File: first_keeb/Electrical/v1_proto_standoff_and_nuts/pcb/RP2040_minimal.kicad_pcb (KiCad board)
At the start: 4 copper layers, 67.1 x 66.8 mm, 77 parts, among them J1 Conn_01x04_Socket, P1 USB-TYPE-C-016, Q1 BSS138, SW3 TS-1187A-B-A-B, SW5 TS-1187A-B-A-B, SW6 BUTT1, SW7 BUTT3, SW8 BUTT2, U1 ME6208A44M3G, U2 ME6206A25XG, U3 PRTR5V0U2X, U5 STM32F401RCTx, U7 SLSS49E, U8 SLSS49E, U9 SLSS49E, Y1 8MHz

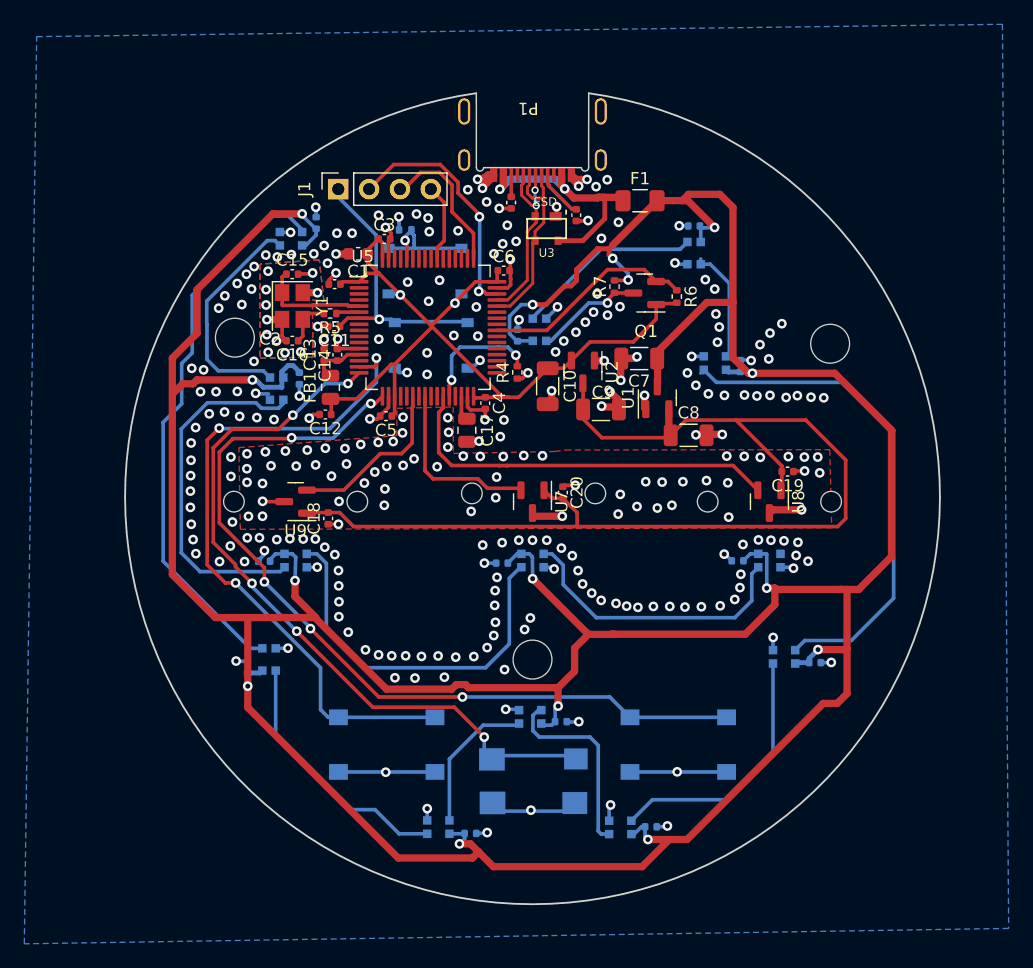
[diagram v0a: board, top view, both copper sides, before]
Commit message: changes to ws2812b 5050 and moves 5v power rail to mostly 4th layer
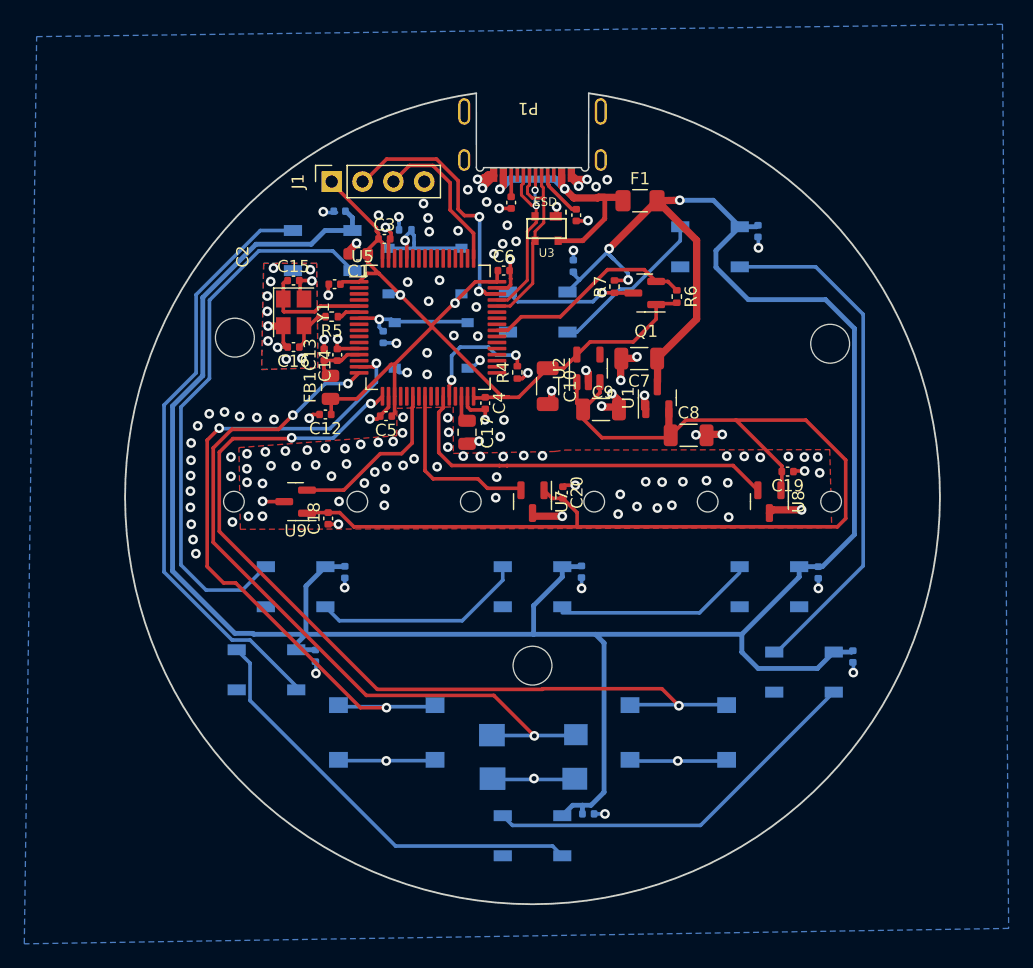
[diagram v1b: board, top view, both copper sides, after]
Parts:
- removed C30, C31, C32, C33: 100n, Capacitor_SMD:C_0402_1005Metric
- removed D10, D11, D12, D13: WS2812B-2020, LED_SMD:LED_WS2812B-2020_PLCC4_2.0x2.0mm
- C11: moved to B.Cu
- D1, D2, D3, D4, D5, D6, D7, D8, D9: value WS2812B-2020 -> WS2812B; footprint LED_SMD:LED_WS2812B-2020_PLCC4_2.0x2.0mm -> LED_SMD:LED_WS2812B_PLCC4_5.0x5.0mm_P3.2mm
- U2: value ME6206A25XG -> ME6212C33M5G; footprint Package_TO_SOT_SMD:SOT-23 -> Package_TO_SOT_SMD:SOT-23-5
- moved C25 49.8 mm to (118.6, 77.7), turned to -90 degrees
- moved D5 48.4 mm to (114.6, 79.0), turned to 180 degrees
- moved C24 38.2 mm to (103.4, 80.6), turned to 90 degrees
- moved D4 34.9 mm to (100.4, 84.4), turned to 180 degrees
- moved D2 30.5 mm to (100.0, 107.0), turned to 180 degrees
- moved C22 29.9 mm to (104.0, 105.8), turned to -90 degrees
- moved D1 29.2 mm to (80.5, 107.0), turned to 180 degrees
- moved C26 24.6 mm to (126.4, 112.8), turned to -90 degrees
- moved C21 24.1 mm to (84.5, 105.8), turned to -90 degrees
- moved D6 22.8 mm to (122.3, 114.0), turned to 180 degrees
- moved D3 18.9 mm to (119.5, 107.0), turned to 180 degrees
- moved C23 18.2 mm to (123.5, 105.8), turned to -90 degrees
- moved C27 9.83 mm to (104.6, 125.7)
- moved D7 7.79 mm to (100.0, 127.5), turned to 180 degrees
- moved C28 5.67 mm to (82.1, 112.7), turned to -90 degrees
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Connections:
- D1 pad 1: Net-(D1-DOUT) -> +5V
- D1 pad 2: GND -> Net-(D1-DOUT)
- D1 pad 3: Net-(D1-DIN) -> GND
- D1 pad 4: +5V -> UG_DIN
- D2 pad 1: Net-(D2-DOUT) -> +5V
- D2 pad 2: GND -> Net-(D2-DOUT)
- D2 pad 3: Net-(D1-DOUT) -> GND
- D2 pad 4: +5V -> Net-(D1-DOUT)
- D3 pad 1: Net-(D3-DOUT) -> +5V
- D3 pad 2: GND -> unconnected-(D3-DOUT-Pad2)
- D3 pad 3: Net-(D2-DOUT) -> GND
- D3 pad 4: +5V -> Net-(D2-DOUT)
- D4 pad 1: Net-(D4-DOUT) -> +5V
- D4 pad 2: GND -> Net-(D4-DOUT)
- D4 pad 3: Net-(D3-DOUT) -> GND
- D4 pad 4: +5V -> Net-(D4-DIN)
- D5 pad 1: Net-(D5-DOUT) -> +5V
- D5 pad 2: GND -> Net-(D5-DOUT)
- D5 pad 3: Net-(D4-DOUT) -> GND
- D5 pad 4: +5V -> Net-(D4-DOUT)
- D6 pad 1: Net-(D6-DOUT) -> +5V
- D6 pad 2: GND -> Net-(D6-DOUT)
- D6 pad 3: Net-(D5-DOUT) -> GND
- D6 pad 4: +5V -> Net-(D5-DOUT)
- D7 pad 1: Net-(D7-DOUT) -> +5V
- D7 pad 2: GND -> Net-(D7-DOUT)
- D7 pad 3: Net-(D6-DOUT) -> GND
- D7 pad 4: +5V -> Net-(D6-DOUT)
- D8 pad 1: Net-(D8-DOUT) -> +5V
- D8 pad 2: GND -> Net-(D8-DOUT)
- D8 pad 3: Net-(D7-DOUT) -> GND
- D8 pad 4: +5V -> Net-(D7-DOUT)
- D9 pad 1: Net-(D10-DIN) -> +5V
- D9 pad 2: GND -> UG_DIN
- D9 pad 3: Net-(D8-DOUT) -> GND
- D9 pad 4: +5V -> Net-(D8-DOUT)
- J1 pad 1: NRST -> VDD
- J1 pad 4: SWO -> GND
- Q1 pad 3: Net-(D1-DIN) -> Net-(D4-DIN)
- R7 pad 1: Net-(D1-DIN) -> Net-(D4-DIN)
- U2 pad 1: GND -> +4V4
- U2 pad 2: VDD -> GND
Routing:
- net +5V: track 334.4 -> 229.8 mm, vias 15 -> 3
- net UG_DIN: track 0.00 -> 45.5 mm
- net Net-(D3-DOUT): track 41.7 -> 0.00 mm
- net Net-(D11-DOUT): track 31.2 -> 0.00 mm
- net Net-(D10-DOUT): track 29.4 -> 0.00 mm
- net Net-(D5-DOUT): track 16.1 -> 42.7 mm
- net Net-(D12-DOUT): track 23.8 -> 0.00 mm
- net Net-(D6-DOUT): track 12.0 -> 32.1 mm
- net Net-(D10-DIN): track 18.9 -> 0.00 mm
- net GND: track 113.7 -> 95.9 mm, vias 294 -> 158
- net Net-(D7-DOUT): track 21.1 -> 35.6 mm
- net NRST: track 23.1 -> 10.3 mm
- net Net-(D4-DIN): track 0.00 -> 10.9 mm, vias 0 -> 1
- net Net-(D1-DIN): track 8.94 -> 0.00 mm, vias 1 -> 0
- net Net-(D4-DOUT): track 21.3 -> 13.5 mm
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
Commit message: v1 stm ordered
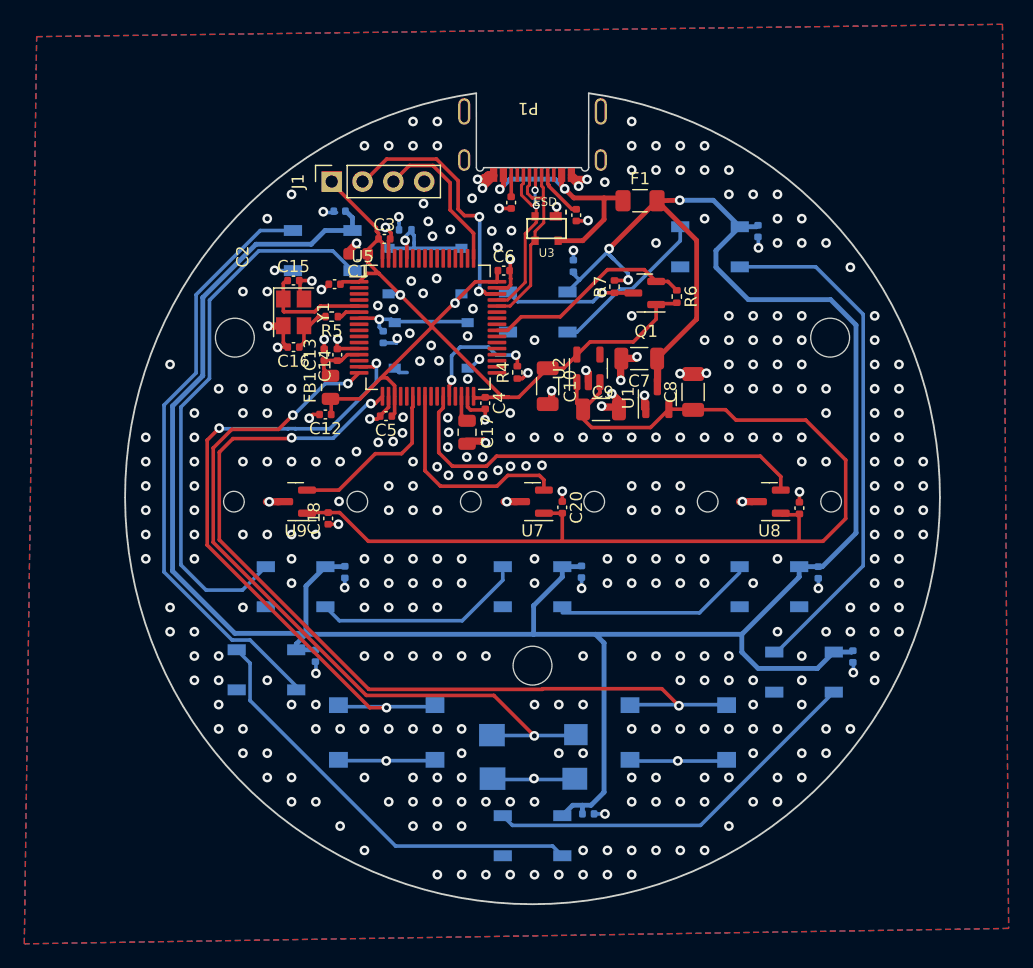
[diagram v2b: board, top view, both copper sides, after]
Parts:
- U2: value ME6212C33M5G -> ME6212C25M5G
- moved C8 3.59 mm to (113.2, 91.0), turned to 90 degrees
- moved C19 3.16 mm to (122.0, 100.5), turned to -90 degrees
- moved C20 1.22 mm to (102.5, 100.5)
- moved H1 0.50 mm to (124.5, 86.5)
- turned U7 to 180 degrees
- turned U8 to 180 degrees
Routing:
- net +4V4: track 93.4 -> 88.0 mm
- net ADC_IN3: track 32.3 -> 35.6 mm
- net ADC_IN2: track 14.7 -> 17.8 mm
- net BUTT0: track 57.2 -> 56.2 mm
- net GND: track 95.9 -> 95.3 mm, vias 158 -> 376

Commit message: updates pcb
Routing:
- net Net-(D2-DOUT): track 16.0 -> 17.0 mm
- net GND: track 95.3 -> 95.6 mm, vias 376 -> 381
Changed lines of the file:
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@@
   (segment (start 78.29 99.97) (end 78.24 99.97) (width 0.3) (layer "F.Cu") (net 1))
   (segment (start 103.8 73.95) (end 103.72 73.87) (width 0.3) (layer "F.Cu") (net 1))
+  (segment (start 101.854 75.692) (end 101.985023 75.823023) (width 0.4) (layer "F.Cu") (net 1))
   (segment (start 103.569466 73.474466) (end 103.2 73.105) (width 0.6) (layer "F.Cu") (net 1))
   (segment (start 101.575 90.875) (end 101.575 91.943813) (width 0.6) (layer "F.Cu") (net 1))
@@
   (segment (start 88.355 77.88) (end 88.355 78.3) (width 0.3) (layer "F.Cu") (net 1))
   (segment (start 104.375 76.895) (end 104.57 76.86) (width 0.3) (layer "F.Cu") (net 1))
+  (segment (start 101.985023 75.823023) (end 101.985023 76.325023) (width 0.4) (layer "F.Cu") (net 1))
   (segment (start 98.17 80.05) (end 98.17 81.168959) (width 0.3) (layer "F.Cu") (net 1))
   (segment (start 98.242 75.863) (end 97.313 75.863) (width 0.3) (layer "F.Cu") (net 1))
@@
   (segment (start 96.8 73.22) (end 95.88 74.14) (width 0.6) (layer "F.Cu") (net 1))
   (segment (start 97.951041 82.4) (end 97.075 82.4) (width 0.3) (layer "F.Cu") (net 1))
-  (segment (start 101.985023 75.724977) (end 101.985023 76.325023) (width 0.4) (layer "F.Cu") (net 1))
   (segment (start 106.5275 91.1025) (end 107.04 91.615) (width 0.6) (layer "F.Cu") (net 1))
   (segment (start 81.808258 81.798258) (end 80.802728 81.798258) (width 0.3) (layer "F.Cu") (net 1))
@@
   (via (at 90.166 108.706) (size 0.8) (drill 0.4) (layers "F.Cu" "B.Cu") (free) (net 1))
   (via (at 124.166 118.706) (size 0.8) (drill 0.4) (layers "F.Cu" "B.Cu") (free) (net 1))
+  (via (at 108.166 108.706) (size 0.8) (drill 0.4) (layers "F.Cu" "B.Cu") (free) (net 1))
   (via (at 101.575 90.875) (size 0.8) (drill 0.4) (layers "F.Cu" "B.Cu") (net 1))
   (via (at 100.166 104.706) (size 0.8) (drill 0.4) (layers "F.Cu" "B.Cu") (free) (net 1))
@@
   (via (at 90.166 70.706) (size 0.8) (drill 0.4) (layers "F.Cu" "B.Cu") (free) (net 1))
   (via (at 117.28 100) (size 0.8) (drill 0.4) (layers "F.Cu" "B.Cu") (net 1))
+  (via (at 112.166 108.706) (size 0.8) (drill 0.4) (layers "F.Cu" "B.Cu") (free) (net 1))
+  (via (at 104.166 108.706) (size 0.8) (drill 0.4) (layers "F.Cu" "B.Cu") (free) (net 1))
   (via (at 100.166 106.706) (size 0.8) (drill 0.4) (layers "F.Cu" "B.Cu") (free) (net 1))
   (via (at 76.166 92.706) (size 0.8) (drill 0.4) (layers "F.Cu" "B.Cu") (free) (net 1))
-  (via (at 103.37 79.3195) (size 0.8) (drill 0.4) (layers "F.Cu" "B.Cu") (net 1))
+  (via (at 104.394 80.01) (size 0.8) (drill 0.4) (layers "F.Cu" "B.Cu") (net 1))
   (via (at 68.166 104.706) (size 0.8) (drill 0.4) (layers "F.Cu" "B.Cu") (free) (net 1))
   (via (at 72.166 96.706) (size 0.8) (drill 0.4) (layers "F.Cu" "B.Cu") (free) (net 1))
@@
   (via (at 91 82.85) (size 0.8) (drill 0.4) (layers "F.Cu" "B.Cu") (free) (net 1))
   (via (at 87.27 83.86) (size 0.8) (drill 0.4) (layers "F.Cu" "B.Cu") (free) (net 1))
-  (via (at 101.985023 75.724977) (size 0.8) (drill 0.4) (layers "F.Cu" "B.Cu") (net 1))
+  (via (at 101.854 75.692) (size 0.8) (drill 0.4) (layers "F.Cu" "B.Cu") (net 1))
   (via (at 78.166 82.706) (size 0.8) (drill 0.4) (layers "F.Cu" "B.Cu") (free) (net 1))
   (via (at 108.166 94.706) (size 0.8) (drill 0.4) (layers "F.Cu" "B.Cu") (free) (net 1))
@@
   (via (at 82.85 86.64) (size 0.8) (drill 0.4) (layers "F.Cu" "B.Cu") (net 1))
   (via (at 108.166 68.706) (size 0.8) (drill 0.4) (layers "F.Cu" "B.Cu") (free) (net 1))
+  (via (at 106.166 108.706) (size 0.8) (drill 0.4) (layers "F.Cu" "B.Cu") (free) (net 1))
   (via (at 82.166 116.706) (size 0.8) (drill 0.4) (layers "F.Cu" "B.Cu") (free) (net 1))
   (via (at 114.3125 89.4275) (size 0.8) (drill 0.4) (layers "F.Cu" "B.Cu") (net 1))
@@
   (via (at 118.166 124.706) (size 0.8) (drill 0.4) (layers "F.Cu" "B.Cu") (free) (net 1))
   (via (at 120.166 94.706) (size 0.8) (drill 0.4) (layers "F.Cu" "B.Cu") (free) (net 1))
+  (via (at 110.166 108.706) (size 0.8) (drill 0.4) (layers "F.Cu" "B.Cu") (free) (net 1))
   (via (at 78.166 92.706) (size 0.8) (drill 0.4) (layers "F.Cu" "B.Cu") (free) (net 1))
   (via (at 68.166 100.706) (size 0.8) (drill 0.4) (layers "F.Cu" "B.Cu") (free) (net 1))
@@
   (segment (start 123.535 106.245) (end 123.535 107.135) (width 0.3) (layer "B.Cu") (net 1))
   (segment (start 123.535 107.145) (end 123.535 107.195) (width 0.3) (layer "B.Cu") (net 1))
-  (segment (start 103.37 79.3195) (end 103.37 80.18) (width 0.3) (layer "B.Cu") (net 1))
   (segment (start 126.41 114.07) (end 126.415 114.075) (width 0.3) (layer "B.Cu") (net 1))
   (segment (start 88.86 86.56) (end 88.8 86.96) (width 0.3) (layer "B.Cu") (net 1))
   (segment (start 87.9425 121.32) (end 84.0675 121.32) (width 0.3) (layer "B.Cu") (net 1))
-  (segment (start 103.37 80.18) (end 103.36 80.19) (width 0.3) (layer "B.Cu") (net 1))
+  (segment (start 103.54 80.01) (end 103.36 80.19) (width 0.3) (layer "B.Cu") (net 1))
   (segment (start 92.0175 121.32) (end 87.9825 121.32) (width 0.3) (layer "B.Cu") (net 1))
+  (segment (start 104.394 80.01) (end 103.54 80.01) (width 0.3) (layer "B.Cu") (net 1))
   (segment (start 104.045 107.135) (end 104.04 107.14) (width 0.3) (layer "B.Cu") (net 1))
   (segment (start 82.17 114.14) (end 82.175 114.145) (width 0.3) (layer "B.Cu") (net 1))
@@
   (segment (start 102.4 74) (end 102.4 73.105) (width 0.4) (layer "F.Cu") (net 2))
   (segment (start 97.31 74.28) (end 97.6 73.99) (width 0.4) (layer "F.Cu") (net 2))
-  (segment (start 104.14 78.52) (end 102.11 78.52) (width 0.4) (layer "F.Cu") (net 2))
   (segment (start 97.32 74.28) (end 97.415 74.185) (width 0.4) (layer "F.Cu") (net 2))
-  (segment (start 105.89 75) (end 105.89 76.77) (width 0.4) (layer "F.Cu") (net 2))
-  (segment (start 105.89 76.77) (end 104.14 78.52) (width 0.4) (layer "F.Cu") (net 2))
+  (segment (start 105.89 76.99) (end 104.36 78.52) (width 0.4) (layer "F.Cu") (net 2))
   (segment (start 102.65 74.25) (end 103.4 75) (width 0.4) (layer "F.Cu") (net 2))
+  (segment (start 105.89 75) (end 105.89 76.99) (width 0.4) (layer "F.Cu") (net 2))
   (segment (start 107.17 74.95) (end 107.45 75.23) (width 0.6) (layer "F.Cu") (net 2))
   (segment (start 107.22 75) (end 107.45 75.23) (width 0.4) (layer "F.Cu") (net 2))
   (segment (start 102.65 74.25) (end 102.4 74) (width 0.4) (layer "F.Cu") (net 2))
   (segment (start 103.4 75) (end 107.22 75) (width 0.4) (layer "F.Cu") (net 2))
+  (segment (start 104.36 78.52) (end 102.11 78.52) (width 0.4) (layer "F.Cu") (net 2))
   (segment (start 97.31 74.28) (end 97.32 74.28) (width 0.4) (layer "F.Cu") (net 2))
   (via (at 102.65 74.25) (size 0.8) (drill 0.4) (layers "F.Cu" "B.Cu") (net 2))
@@
   (segment (start 117.06 80.67) (end 123.31 80.67) (width 0.3) (layer "B.Cu") (net 7))
   (segment (start 127.22 84.58) (end 127.22 105.28) (width 0.3) (layer "B.Cu") (net 7))
-  (segment (start 101.365 74.045) (end 103.255 75.935) (width 0.3) (layer "F.Cu") (net 8))
-  (segment (start 101.365 73.959365) (end 101.365 74.045) (width 0.3) (layer "F.Cu") (net 8))
+  (segment (start 101.25 73.844364) (end 101.9 74.494364) (width 0.3) (layer "F.Cu") (net 8))
   (segment (start 101.25 73.105) (end 101.25 73.844364) (width 0.3) (layer "F.Cu") (net 8))
-  (segment (start 101.25 73.844364) (end 101.365 73.959365) (width 0.3) (layer "F.Cu") (net 8))
-  (segment (start 103.255 75.935) (end 103.6 75.935) (width 0.3) (layer "F.Cu") (net 8))
+  (segment (start 101.9 74.560661) (end 103.274339 75.935) (width 0.3) (layer "F.Cu") (net 8))
+  (segment (start 101.9 74.494364) (end 101.9 74.560661) (width 0.3) (layer "F.Cu") (net 8))
+  (segment (start 103.274339 75.935) (end 103.6 75.935) (width 0.3) (layer "F.Cu") (net 8))
   (segment (start 98.25 73.105) (end 98.25 74.895) (width 0.3) (layer "F.Cu") (net 9))
   (segment (start 98.25 74.895) (end 98.242 74.903) (width 0.3) (layer "F.Cu") (net 9))
@@
   (segment (start 98.78 83.54) (end 97.98 82.74) (width 0.3) (layer "B.Cu") (net 28))
   (segment (start 104.969954 83.54) (end 98.78 83.54) (width 0.3) (layer "B.Cu") (net 28))
-  (segment (start 113.75 109.15) (end 117.05 105.85) (width 0.3) (layer "B.Cu") (net 29))
-  (segment (start 102.45 109.15) (end 113.75 109.15) (width 0.3) (layer "B.Cu") (net 29))
+  (segment (start 117.05 106.47) (end 117.05 105.85) (width 0.3) (layer "B.Cu") (net 29))
+  (segment (start 113.538 109.982) (end 117.05 106.47) (width 0.3) (layer "B.Cu") (net 29))
+  (segment (start 103.282 109.982) (end 113.538 109.982) (width 0.3) (layer "B.Cu") (net 29))
+  (segment (start 102.45 109.15) (end 103.282 109.982) (width 0.3) (layer "B.Cu") (net 29))
   (segment (start 77.467818 79.36) (end 73.41 83.417818) (width 0.3) (layer "B.Cu") (net 30))
   (segment (start 71.06 105.21) (end 73.13 107.28) (width 0.3) (layer "B.Cu") (net 30))
@@
       39af1b7c-ce36-4d43-b79c-db0325fb8ad9
       3b57abf6-9ccd-47e5-a6c3-8e7e6bc16ece
+      3c3f6431-7c09-4b53-96ac-280268f572f1
       3e16085b-648a-4861-b5b0-3a28b1d98fd8
       3e9e9a47-c3de-4e00-b947-a3762355014b
@@
       5fb3cd9b-1a7b-4f30-9b57-30580213a19d
       5fcf152a-7056-45c5-a445-d560a1e74efd
+      630f6a37-6da4-4ba7-ac45-6c41674b1b24
+      63565607-6423-4639-bef8-99f6b9146916
       63cfac18-6b2d-4f65-bd1a-733277dafeb4
       640b6275-e420-426d-9ae9-7b2172bce8c6
@@
       947bb66d-c82f-491f-b1ac-00a6f4a9539b
       96adf5cc-65ac-4ea0-b106-55fa4dbad368
+      9719af89-5fc9-497e-8b3c-e8d4a4ebd2a7
       989a341c-d69c-400c-bbe3-20ae81fc39a7
       9a905659-6a8e-4758-a68d-0cf5c1384203
@@
       a94d6ade-2327-4686-afc5-2f2d60522619
       aab95d37-fc69-4ff3-8015-c214b037ee7f
+      ab72256c-b2c1-45f0-96ee-217147a384e7
       ab8100eb-ac50-4d5d-9f81-ef9378e58a4b
       ac239ae2-b136-4d6e-9265-5eb5efb93554
